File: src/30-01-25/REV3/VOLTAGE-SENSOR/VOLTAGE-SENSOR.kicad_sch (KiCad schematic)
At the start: 83 parts, among them U1 LM324, U2 zmpt101b, U6 zmpt101b, U7 LM324, U8 zmpt101b, U9 LM324

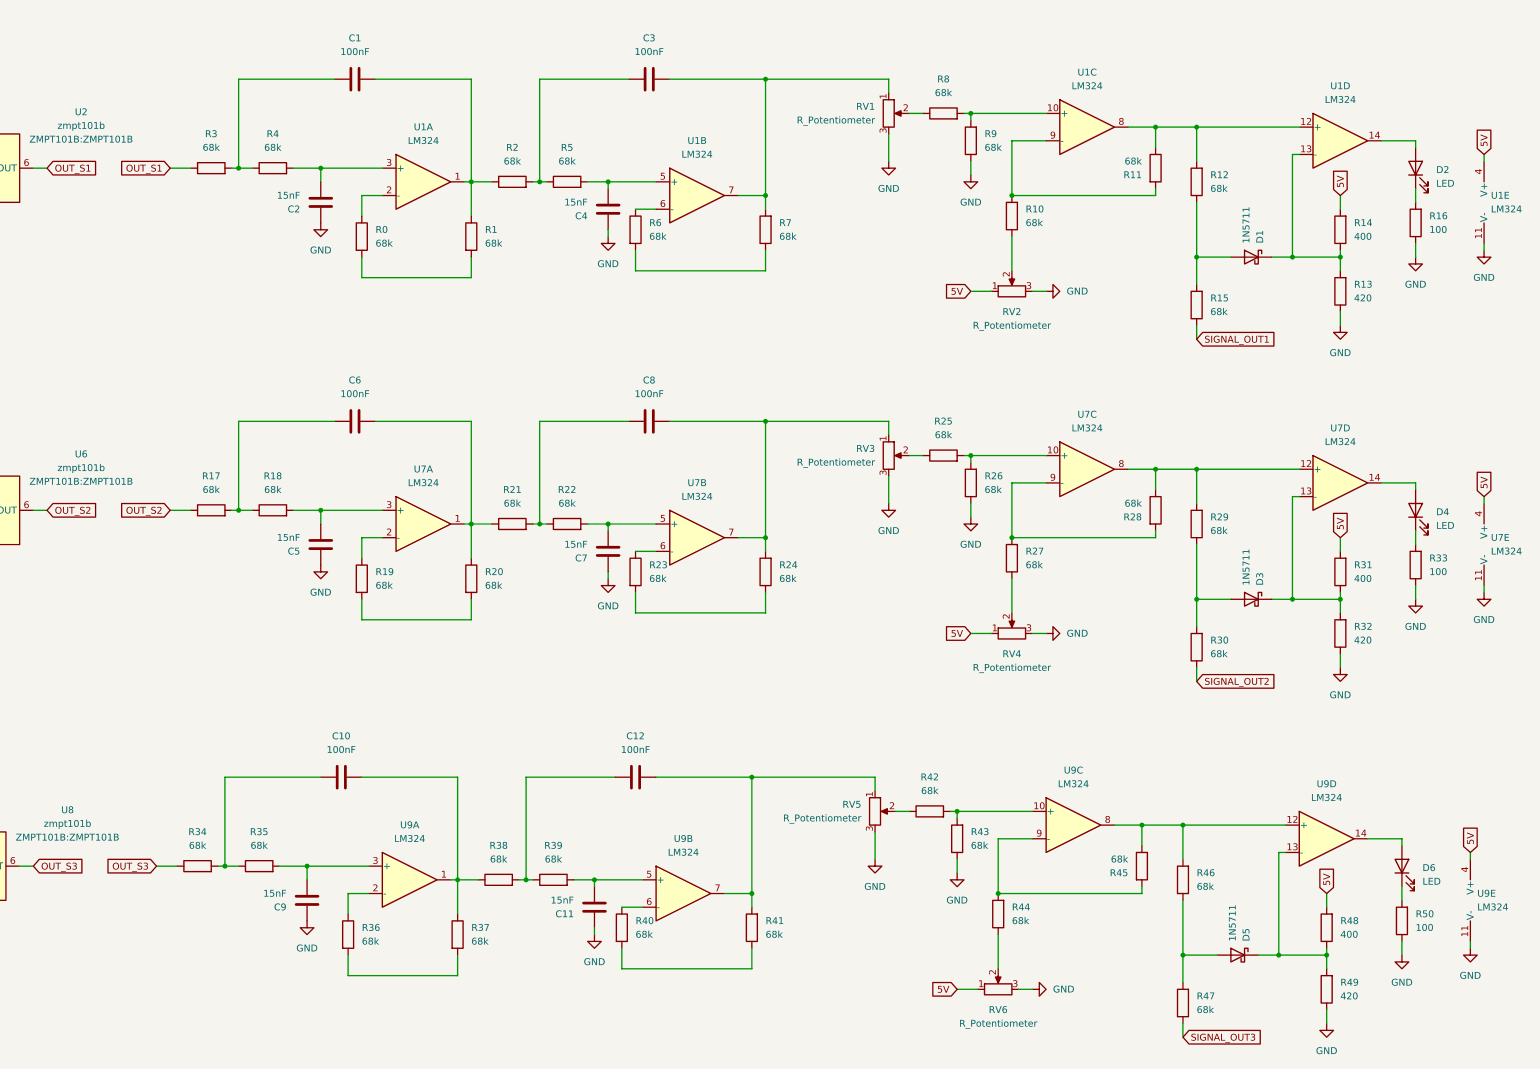
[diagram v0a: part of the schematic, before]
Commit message: Change: reading data by polling
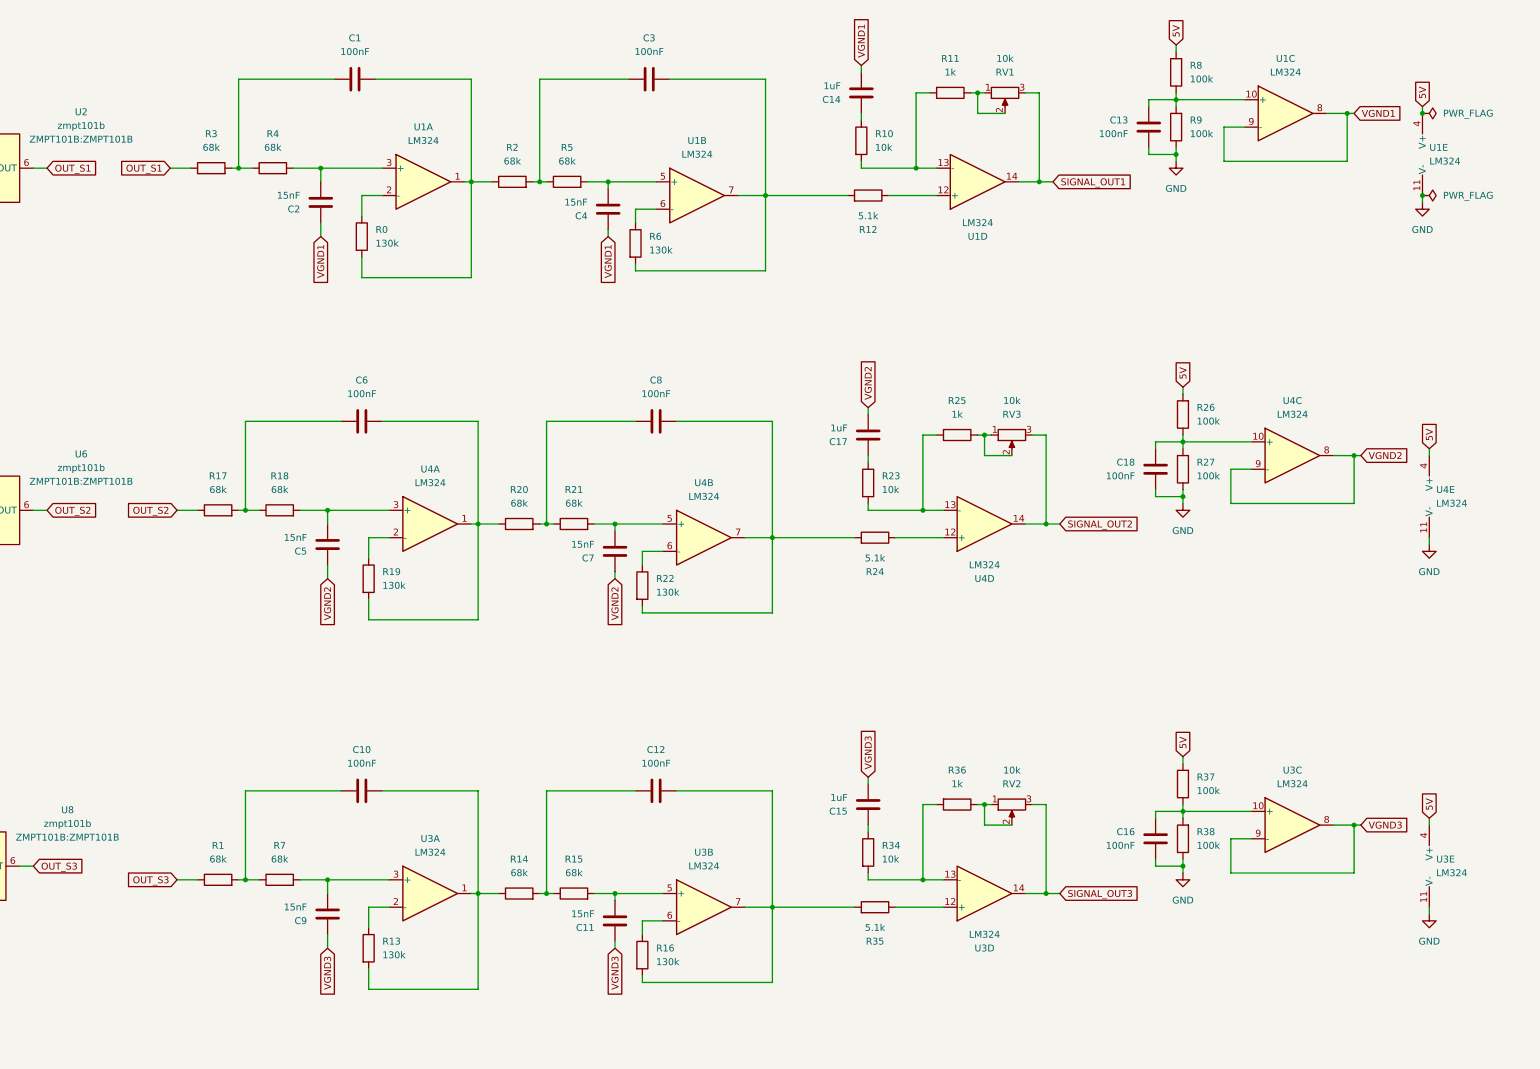
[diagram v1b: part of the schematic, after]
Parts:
- removed D1, D3, D5: 1N5711, Diode_THT:D_DO-35_SOD27_P7.62mm_Horizontal, symbol Diode:1N5711
- removed D2, D4, D6: LED, LED_THT:LED_D4.0mm, symbol Device:LED
- removed R28, R29, R30, R39, R40, R41, R42, R43, R44, R45, R46, R47: 68k, Resistor_THT:R_Axial_DIN0207_L6.3mm_D2.5mm_P7.62mm_Horizontal, symbol DIY:R
- removed R31, R48: 400, Resistor_THT:R_Axial_DIN0207_L6.3mm_D2.5mm_P7.62mm_Horizontal, symbol DIY:R
- removed R32, R49: 420, Resistor_THT:R_Axial_DIN0207_L6.3mm_D2.5mm_P7.62mm_Horizontal, symbol DIY:R
- removed R33, R50: 100, Resistor_THT:R_Axial_DIN0207_L6.3mm_D2.5mm_P7.62mm_Horizontal, symbol DIY:R
- removed RV4, RV5, RV6: R_Potentiometer, Potentiometer_THT:Potentiometer_Bourns_3296W_Vertical, symbol Device:R_Potentiometer
- removed U7, U9: LM324, Package_DIP:DIP-14_W7.62mm_LongPads, symbol Amplifier_Operational:LM324
- added C13, C16, C18: 100nF, Capacitor_THT:C_Rect_L11.0mm_W4.3mm_P10.00mm_MKT, symbol Device:C
- added C14, C15, C17: 1uF, Capacitor_THT:C_Rect_L7.0mm_W2.5mm_P5.00mm, symbol Device:C
- added U3, U4: LM324, Package_DIP:DIP-14_W7.62mm_LongPads, symbol Amplifier_Operational:LM324
- R0, R19, R22, R6: value 68k -> 130k
- R10, R23, R34: value 68k -> 10k
- R11, R25, R36: value 68k -> 1k
- R12, R24, R35: value 68k -> 5.1k
- R13: value 420 -> 130k
- R14: value 400 -> 68k
- R16: value 100 -> 130k
- R26, R27, R37, R38, R8, R9: value 68k -> 100k
- RV1, RV2, RV3: value R_Potentiometer -> 10k
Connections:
- net 5V: now also R26.2, R37.2, R8.2, U3.4 (V+), U4.4 (V+); no longer R14.2, RV2.1
- net GND: now also R27.1, R38.1, C13.1, C16.1, C18.1, U3.11 (V-), U4.11 (V-); no longer C11.1, C2.1, C4.1, C5.1, C7.1, C9.1, R13.1, R16.1, R26.1, RV1.3, RV2.3, RV3.3
- net OUT_S3: now also R1.1; no longer R34.1
- net SIGNAL_OUT1: now also RV1.3, U1.14; no longer R15.1
- net SIGNAL_OUT2: now also RV3.3, U4.14
- net SIGNAL_OUT3: now also RV2.3, U3.14
- net at R9.2, U1.10 (+): now also R8.1, C13.2; no longer R8.2
- net at R25.2: now also R23.2, U4.13 (-); no longer R26.2
- net at R27.2: now also R26.1, C18.2, U4.10 (+)
- net at C9.2: now also R7.2, U3.3 (+); no longer R35.2
- net at R19.1: now also U4.2 (-)
- net at R19.2: now also C6.2, R20.1, U4.1; no longer R20.2
- net at C1.2, R2.1, U1.1: now also R0.2; no longer R1.1
- net at R1.2: now also C10.1, R7.1; no longer R0.2
- net at C3.2, U1.7: now also R12.2, R6.2; no longer R7.2, RV1.1
- net at C12.2: now also R16.2, R35.2, U3.7
- net at R10.1: now also C14.1; no longer RV2.2
- net at C8.2, R24.2: now also R22.2, U4.7; no longer RV3.1
- net at C11.2: now also R15.2, U3.5 (+)
- net at C5.2, R18.2: now also U4.3 (+)
- net at R38.2: now also R37.1, C16.2, U3.10 (+); no longer C12.1
- net at R13.2, R14.1: now also C10.2, U3.1; no longer U1.13 (-)
- net at RV1.2: now also R11.1, RV1.1; no longer R8.1
- net at R23.1: now also C17.1
- net at R24.1: now also U4.12 (+); no longer R23.2
- net at R10.2, R11.2: now also U1.13 (-); no longer U1.9 (-)
- net at R36.1: now also RV2.1, RV2.2
- net at R12.1: now also U1.12 (+); no longer R15.2
- net at C7.2: now also R21.2, U4.5 (+); no longer R22.2
- net at R25.1, RV3.2: now also RV3.1
- net at R36.2: now also R34.2, U3.13 (-); no longer R37.2
- new net: C12.1, R14.2, R15.1
- new net: C8.1, R20.2, R21.1
- new net: C15.1, R34.1
- new net: R22.1, U4.6 (-)
- new net: R13.1, U3.2 (-)
- new net: R16.1, U3.6 (-)
- new net: R35.1, U3.12 (+)
- new net VGND1: C14.2, C2.1, C4.1, U1.8, U1.9 (-)
- new net VGND2: C17.2, C5.1, C7.1, U4.8, U4.9 (-)
- new net VGND3: C11.1, C15.2, C9.1, U3.8, U3.9 (-)
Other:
- moved on the sheet: R6, U1C, U1D, U1E
